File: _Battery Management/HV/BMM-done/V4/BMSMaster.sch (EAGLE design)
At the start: 124 parts, among them J1 M2S02B-PASK-2(LF)(SN), J10 IMD, J14 USB_B_RA, J2 M2S02B-PASK-2(LF)(SN), J3 M8S08B-PASK-2(LF)(SN), J5 M16_M_194280016, J6 M2770166, J7 M2770166, J8 M2770166, J9 M2770166, K1 ADJ14024, Q1 IRFR9120TRPBF, Q3 BSS123, U1 SN75HVD08DRMSOP, U10 NC7S14M5X, U11 LTC6820, U12 FT24C64A, U2 TPS54386PWPR, U23 NUD3160DMT1G, U3 FT230X, U4 SN74LVC2G241, U5 NC7S14M5X, U6 DSPIC33FJ128GP804, U7 DMG6602SVTQ, U8 LTC6820, U9 MAX823TEUK+T_3.08, Y1 12Mhz

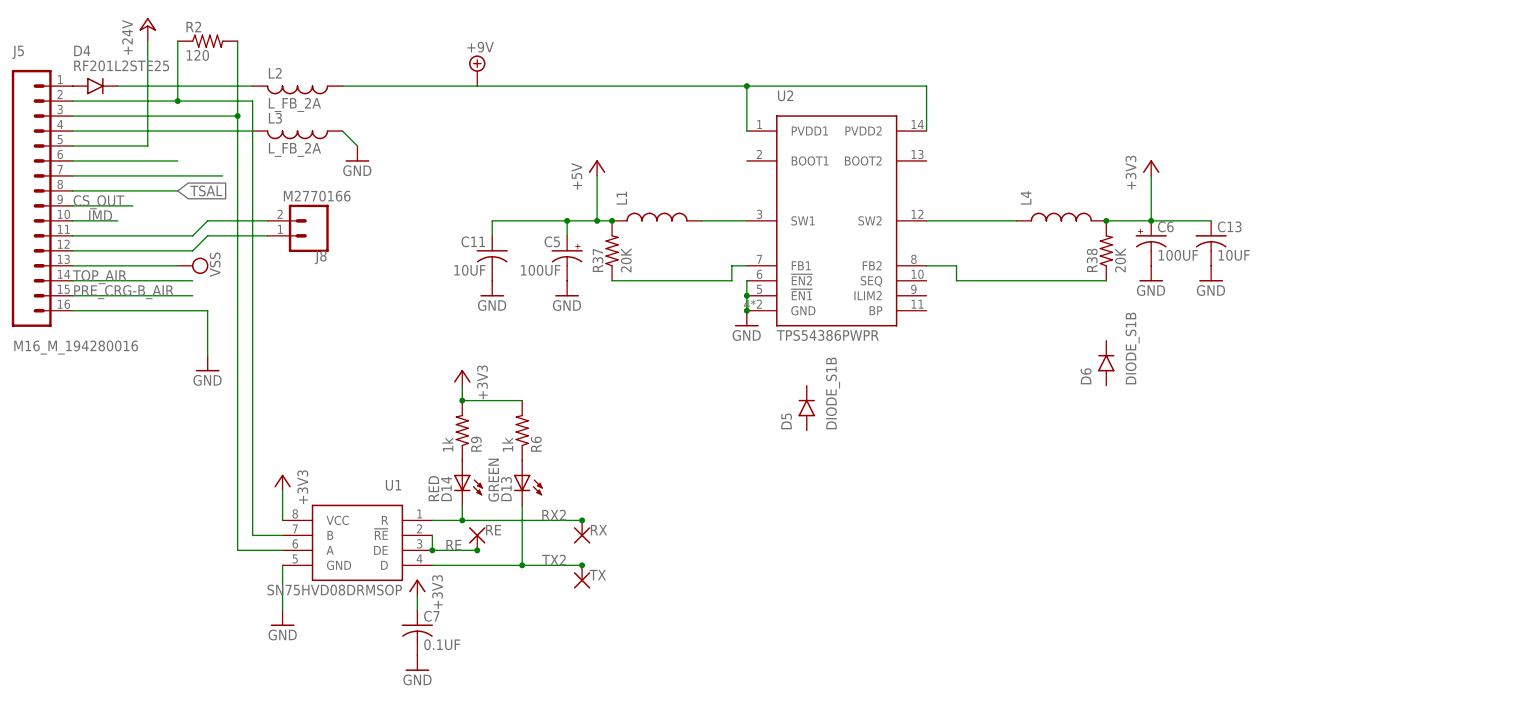
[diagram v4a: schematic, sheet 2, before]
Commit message: 
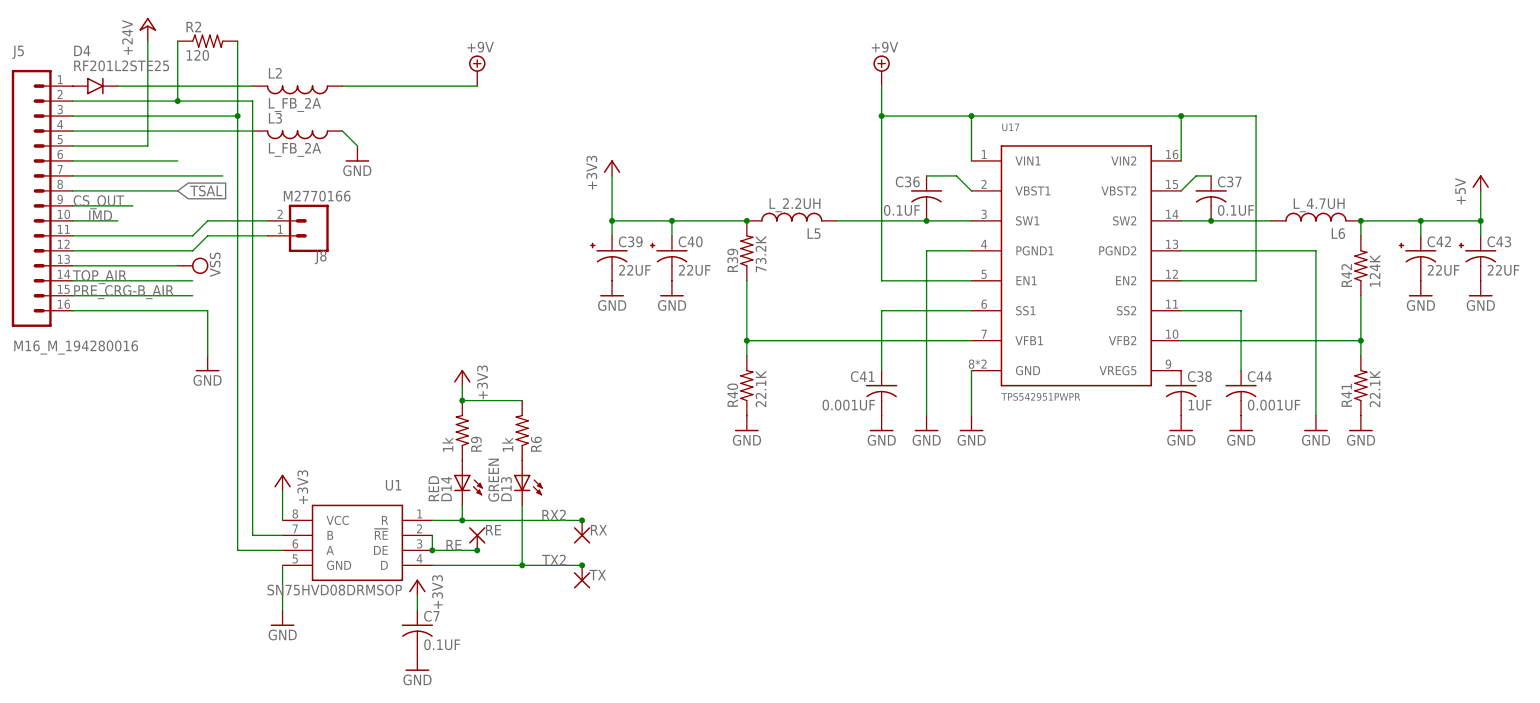
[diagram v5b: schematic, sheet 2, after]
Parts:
- removed C11, C13: 10UF, FSAE Electric:CAP_10UF_50V
- removed C5, C6: 100UF, FSAE Electric:CAP-POL_100UF_50V_SMD
- removed D5, D6: DIODE_S1B, FSAE Electric:DIODE_S1B
- removed L1, L4: (no value), FSAE Electric:INDUCTOR-220MR62
- removed R37, R38: 20K, FSAE Electric:RES_20K_1%_0805
- removed U2: TPS54386PWPR, FSAE Electric:TPS54386PWPR
- added C36, C37: 0.1UF, DFT2:C_0.1UF_50V
- added C38: 1UF, DFT2:C_1UF_16V
- added C39, C40, C42, C43: 22UF, DFT2:C-POL_22UF_35V
- added C41, C44: 0.001UF, DFT2:C_0.001UF_50V
- added L5: L_2.2UH, DFT2:L_2.2UH
- added L6: L_4.7UH, DFT2:L_4.7UH
- added R39: 73.2K, DFT2:R_73.2K_1%
- added R40, R41: 22.1K, DFT2:R_22.1K_1%
- added R42: 124K, DFT2:R_124K_1%
- added U17: TPS542951PWPR, DFT2:TPS542951PWPR
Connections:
- removed net N$56: L1.2, U2.SW1
- removed net N$57: L4.1, U2.SW2
- removed net N$59: R37.1, U2.FB1
- removed net N$61: R38.1, U2.FB2
- new net N$100: C38.1, U17.VREG5
- new net N$101: R39.1, R40.2, U17.VFB1
- new net N$102: C41.1, U17.SS1
- new net N$103: R41.2, R42.1, U17.VFB2
- new net N$77: C44.1, U17.SS2
- new net N$94: C36.1, U17.VBST1
- new net N$97: C36.2, L5.2, U17.SW1
- new net N$98: C37.1, U17.VBST2
- new net N$99: C37.2, L6.1, U17.SW2
- net +3V3: now also C39.+, C40.+, L5.1, R39.2; no longer C13.+, C6.+, L4.2, R38.2
- net +5V: now also C42.+, C43.+, L6.2, R42.2; no longer C11.+, C5.+, L1.1, R37.2
- net +9V: now also U17.EN1, U17.EN2, U17.VIN1, U17.VIN2; no longer U2.PVDD1, U2.PVDD2
- net GND: now also C38.2, C39.-, C40.-, C41.2, C42.-, C43.-, C44.2, R40.1, R41.1, U17.GND, U17.PGND1, U17.PGND2; no longer C11.-, C13.-, C5.-, C6.-, U2.!EN1, U2.!EN2, U2.GND
